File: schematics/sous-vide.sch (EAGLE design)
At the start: 30 parts, among them IC1 MEGA32-P

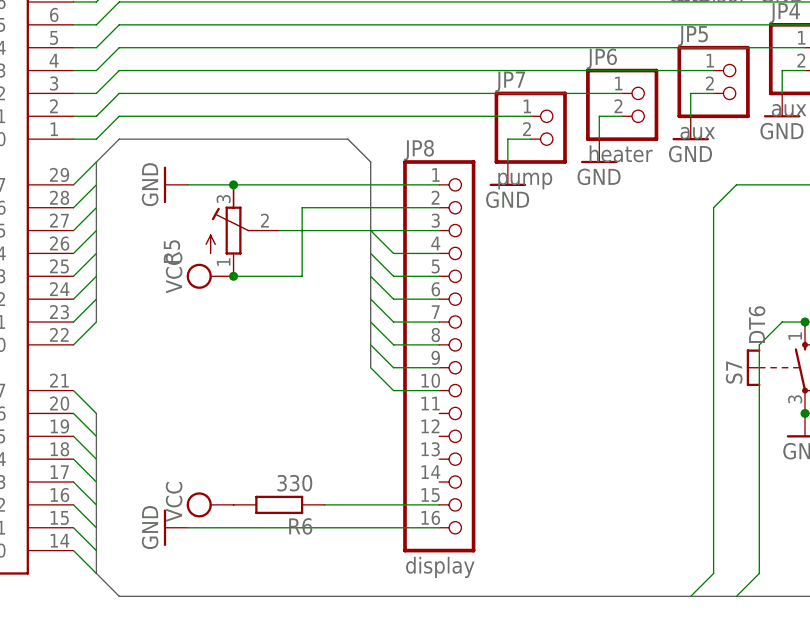
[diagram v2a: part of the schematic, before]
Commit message: initial steps to move from at32u4 naar at32
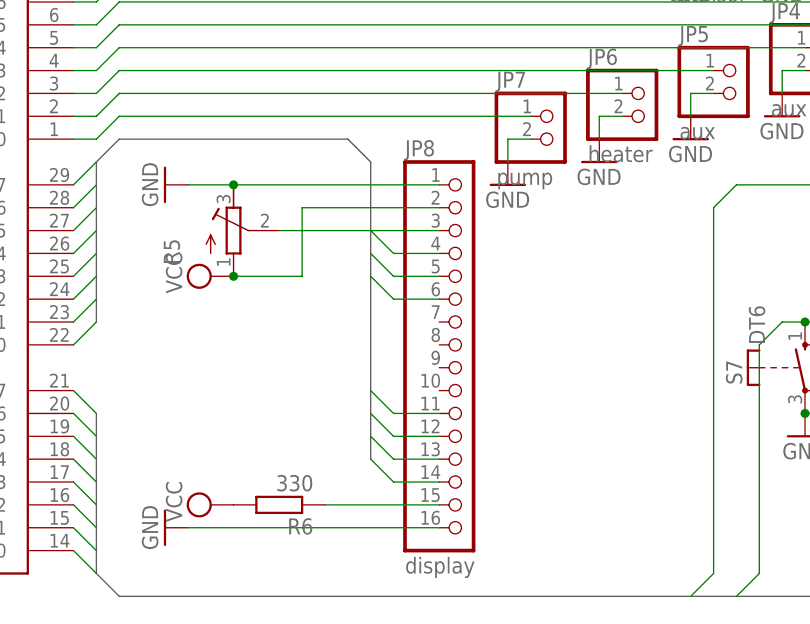
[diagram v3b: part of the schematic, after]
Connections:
- net DISPLAY4: now also JP8.11; no longer JP8.7
- net DISPLAY5: now also JP8.12; no longer JP8.8
- net DISPLAY6: now also JP8.13; no longer JP8.9
- net DISPLAY7: now also JP8.14; no longer JP8.10
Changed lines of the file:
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@@
 <wire x1="63.5" y1="55.88" x2="88.9" y2="55.88" width="0.762" layer="92"/>
 <wire x1="88.9" y1="55.88" x2="91.44" y2="53.34" width="0.762" layer="92"/>
-<wire x1="91.44" y1="53.34" x2="91.44" y2="30.48" width="0.762" layer="92"/>
+<wire x1="91.44" y1="53.34" x2="91.44" y2="20.32" width="0.762" layer="92"/>
 </segment>
 </bus>
@@
 </segment>
 <segment>
-<wire x1="91.44" y1="38.1" x2="93.98" y2="35.56" width="0.1524" layer="91"/>
-<pinref part="JP8" gate="A" pin="7"/>
-<wire x1="93.98" y1="35.56" x2="99.06" y2="35.56" width="0.1524" layer="91"/>
+<wire x1="91.44" y1="27.94" x2="93.98" y2="25.4" width="0.1524" layer="91"/>
+<pinref part="JP8" gate="A" pin="11"/>
+<wire x1="93.98" y1="25.4" x2="99.06" y2="25.4" width="0.1524" layer="91"/>
 </segment>
 </net>
@@
 </segment>
 <segment>
-<wire x1="91.44" y1="35.56" x2="93.98" y2="33.02" width="0.1524" layer="91"/>
-<pinref part="JP8" gate="A" pin="8"/>
-<wire x1="93.98" y1="33.02" x2="99.06" y2="33.02" width="0.1524" layer="91"/>
+<wire x1="91.44" y1="25.4" x2="93.98" y2="22.86" width="0.1524" layer="91"/>
+<pinref part="JP8" gate="A" pin="12"/>
+<wire x1="93.98" y1="22.86" x2="99.06" y2="22.86" width="0.1524" layer="91"/>
 </segment>
 </net>
@@
 </segment>
 <segment>
-<wire x1="91.44" y1="33.02" x2="93.98" y2="30.48" width="0.1524" layer="91"/>
-<pinref part="JP8" gate="A" pin="9"/>
-<wire x1="93.98" y1="30.48" x2="99.06" y2="30.48" width="0.1524" layer="91"/>
+<wire x1="91.44" y1="22.86" x2="93.98" y2="20.32" width="0.1524" layer="91"/>
+<pinref part="JP8" gate="A" pin="13"/>
+<wire x1="93.98" y1="20.32" x2="99.06" y2="20.32" width="0.1524" layer="91"/>
 </segment>
 </net>
@@
 </segment>
 <segment>
-<wire x1="91.44" y1="30.48" x2="93.98" y2="27.94" width="0.1524" layer="91"/>
-<pinref part="JP8" gate="A" pin="10"/>
-<wire x1="93.98" y1="27.94" x2="99.06" y2="27.94" width="0.1524" layer="91"/>
-</segment>
-</net>
+<wire x1="91.44" y1="20.32" x2="93.98" y2="17.78" width="0.1524" layer="91"/>
+<pinref part="JP8" gate="A" pin="14"/>
+<wire x1="93.98" y1="17.78" x2="99.06" y2="17.78" width="0.1524" layer="91"/>
+</segment>
+</net>

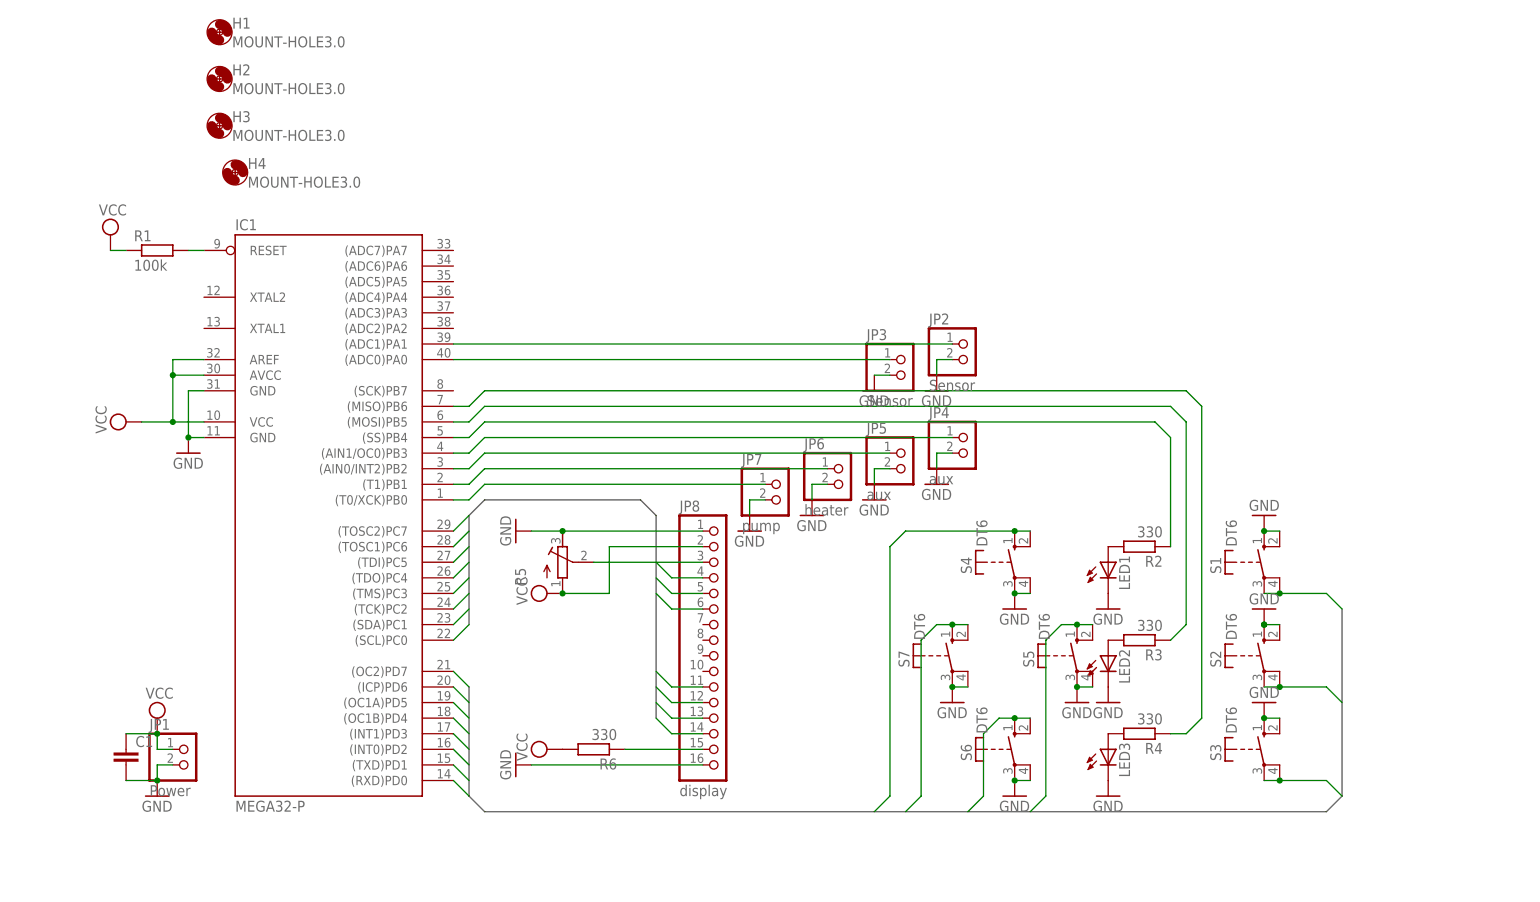
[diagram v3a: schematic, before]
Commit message: Average temp reading + ISP connector
Temp readings are averaged per second before comparing to the set
temperature. Added ISP header to board for on-board reprogramming.
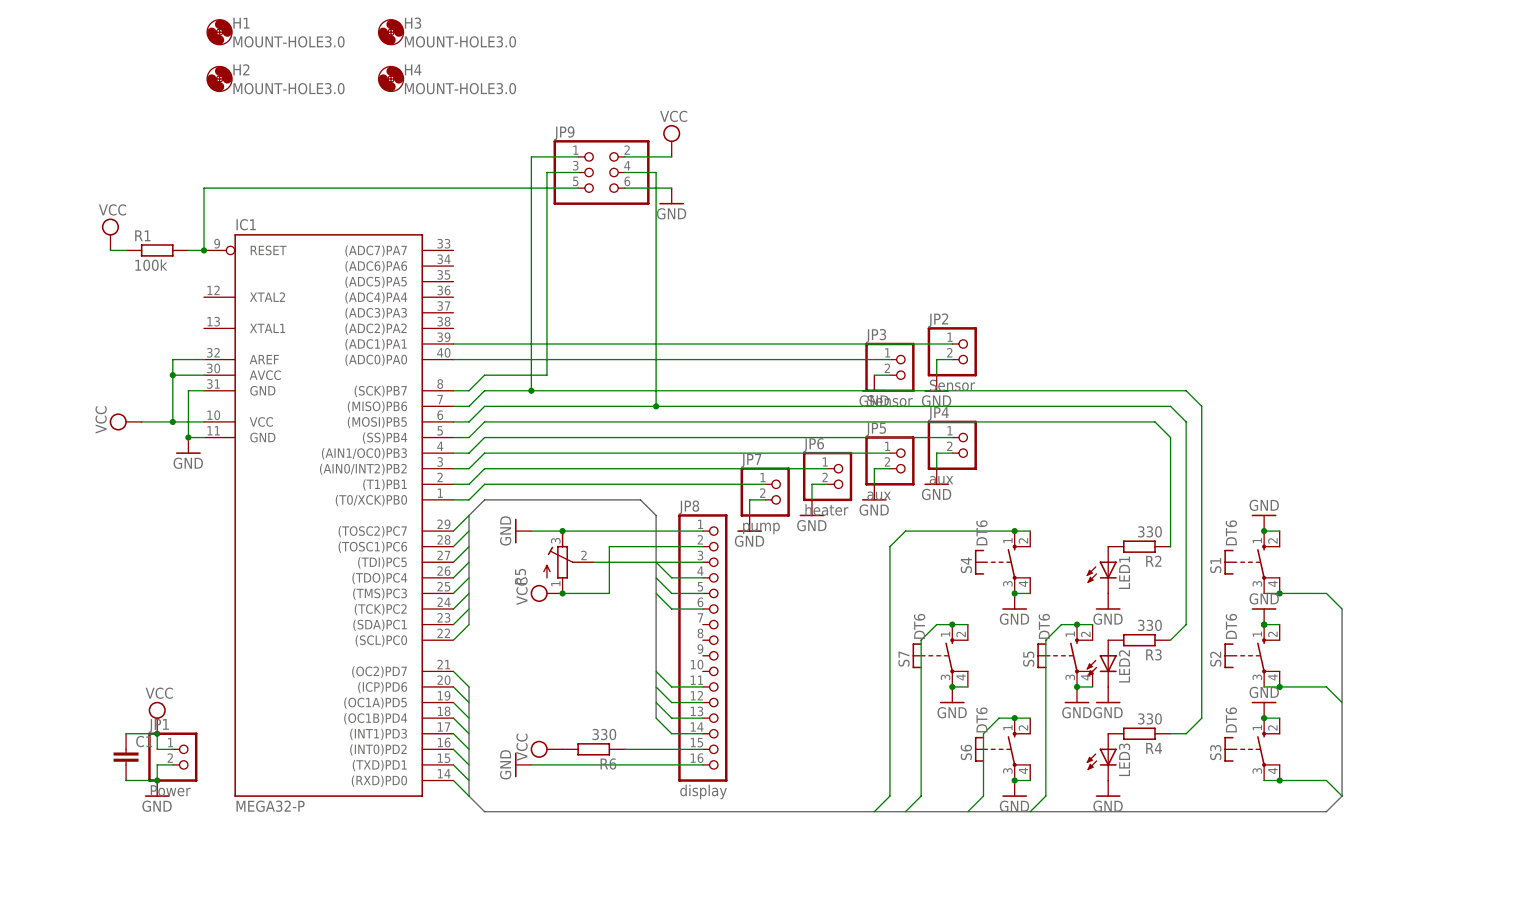
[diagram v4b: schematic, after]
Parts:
- added JP9: (no value), pinhead:PINHD-2X3
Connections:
- new net N$17: IC1.(SCK)PB7, JP9.3
- net GND: now also JP9.6
- net N$11: now also JP9.4
- net N$13: now also JP9.1
- net N$3: now also JP9.5
- net VCC: now also JP9.2
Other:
- moved on the sheet: H3, H4
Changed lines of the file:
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@@
 <part name="GND6" library="supply1" deviceset="GND" device=""/>
 <part name="GND7" library="supply1" deviceset="GND" device=""/>
+<part name="JP9" library="pinhead" deviceset="PINHD-2X3" device=""/>
+<part name="SUPPLY4" library="supply2" deviceset="VCC" device=""/>
+<part name="GND21" library="supply1" deviceset="GND" device=""/>
 </parts>
 <sheets>
@@
 <instance part="H1" gate="G$1" x="20.32" y="132.08"/>
 <instance part="H2" gate="G$1" x="20.32" y="124.46"/>
-<instance part="H3" gate="G$1" x="20.32" y="116.84"/>
-<instance part="H4" gate="G$1" x="22.86" y="109.22"/>
+<instance part="H3" gate="G$1" x="48.26" y="132.08"/>
+<instance part="H4" gate="G$1" x="48.26" y="124.46"/>
 <instance part="GND4" gate="1" x="149.86" y="38.1"/>
 <instance part="GND5" gate="1" x="139.7" y="22.86"/>
 <instance part="GND6" gate="1" x="160.02" y="22.86"/>
 <instance part="GND7" gate="1" x="149.86" y="7.62"/>
+<instance part="JP9" gate="A" x="81.28" y="109.22"/>
+<instance part="SUPPLY4" gate="G$1" x="93.98" y="114.3"/>
+<instance part="GND21" gate="1" x="93.98" y="104.14"/>
 </instances>
 <busses>
@@
 <junction x="149.86" y="10.16"/>
 </segment>
+<segment>
+<pinref part="JP9" gate="A" pin="6"/>
+<pinref part="GND21" gate="1" pin="GND"/>
+<wire x1="93.98" y1="106.68" x2="86.36" y2="106.68" width="0.1524" layer="91"/>
+</segment>
 </net>
 <net name="N$3" class="0">
@@
 <pinref part="R1" gate="G$1" pin="2"/>
 <wire x1="15.24" y1="96.52" x2="17.78" y2="96.52" width="0.1524" layer="91"/>
+<pinref part="JP9" gate="A" pin="5"/>
+<wire x1="78.74" y1="106.68" x2="17.78" y2="106.68" width="0.1524" layer="91"/>
+<wire x1="17.78" y1="106.68" x2="17.78" y2="96.52" width="0.1524" layer="91"/>
+<junction x="17.78" y="96.52"/>
 </segment>
 </net>
@@
 <pinref part="SUPPLY3" gate="G$1" pin="VCC"/>
 </segment>
+<segment>
+<pinref part="JP9" gate="A" pin="2"/>
+<pinref part="SUPPLY4" gate="G$1" pin="VCC"/>
+<wire x1="93.98" y1="111.76" x2="86.36" y2="111.76" width="0.1524" layer="91"/>
+</segment>
 </net>
 <net name="N$12" class="0">
@@
 <wire x1="58.42" y1="68.58" x2="60.96" y2="68.58" width="0.1524" layer="91"/>
 <wire x1="60.96" y1="68.58" x2="63.5" y2="71.12" width="0.1524" layer="91"/>
-<wire x1="63.5" y1="71.12" x2="175.26" y2="71.12" width="0.1524" layer="91"/>
+<wire x1="63.5" y1="71.12" x2="91.44" y2="71.12" width="0.1524" layer="91"/>
+<wire x1="91.44" y1="71.12" x2="175.26" y2="71.12" width="0.1524" layer="91"/>
 <wire x1="175.26" y1="71.12" x2="177.8" y2="68.58" width="0.1524" layer="91"/>
 <pinref part="R3" gate="G$1" pin="1"/>
 <wire x1="177.8" y1="68.58" x2="177.8" y2="35.56" width="0.1524" layer="91"/>
 <wire x1="177.8" y1="35.56" x2="175.26" y2="33.02" width="0.1524" layer="91"/>
+<pinref part="JP9" gate="A" pin="4"/>
+<wire x1="86.36" y1="109.22" x2="91.44" y2="109.22" width="0.1524" layer="91"/>
+<wire x1="91.44" y1="109.22" x2="91.44" y2="71.12" width="0.1524" layer="91"/>
+<junction x="91.44" y="71.12"/>
 </segment>
 </net>
@@
 <wire x1="180.34" y1="20.32" x2="180.34" y2="71.12" width="0.1524" layer="91"/>
 <wire x1="180.34" y1="71.12" x2="177.8" y2="73.66" width="0.1524" layer="91"/>
-<wire x1="177.8" y1="73.66" x2="63.5" y2="73.66" width="0.1524" layer="91"/>
+<wire x1="177.8" y1="73.66" x2="71.12" y2="73.66" width="0.1524" layer="91"/>
+<wire x1="71.12" y1="73.66" x2="63.5" y2="73.66" width="0.1524" layer="91"/>
 <wire x1="63.5" y1="73.66" x2="60.96" y2="71.12" width="0.1524" layer="91"/>
 <pinref part="IC1" gate="G$1" pin="(MISO)PB6"/>
 <wire x1="60.96" y1="71.12" x2="58.42" y2="71.12" width="0.1524" layer="91"/>
+<pinref part="JP9" gate="A" pin="1"/>
+<wire x1="78.74" y1="111.76" x2="71.12" y2="111.76" width="0.1524" layer="91"/>
+<wire x1="71.12" y1="111.76" x2="71.12" y2="73.66" width="0.1524" layer="91"/>
+<junction x="71.12" y="73.66"/>
 </segment>
 </net>
@@
 </segment>
 </net>
+<net name="N$17" class="0">
+<segment>
+<pinref part="JP9" gate="A" pin="3"/>
+<wire x1="78.74" y1="109.22" x2="73.66" y2="109.22" width="0.1524" layer="91"/>
+<wire x1="73.66" y1="109.22" x2="73.66" y2="76.2" width="0.1524" layer="91"/>
+<wire x1="73.66" y1="76.2" x2="63.5" y2="76.2" width="0.1524" layer="91"/>
+<wire x1="63.5" y1="76.2" x2="60.96" y2="73.66" width="0.1524" layer="91"/>
+<pinref part="IC1" gate="G$1" pin="(SCK)PB7"/>
+<wire x1="60.96" y1="73.66" x2="58.42" y2="73.66" width="0.1524" layer="91"/>
+</segment>
+</net>

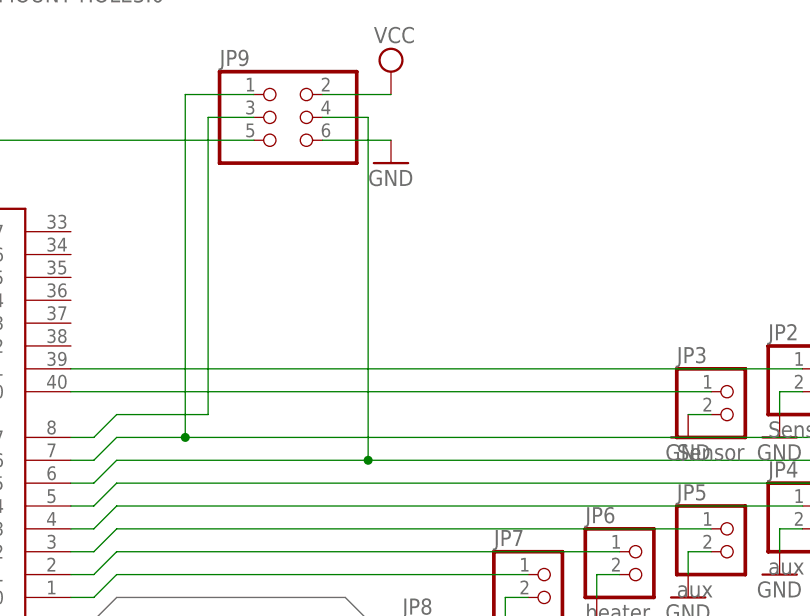
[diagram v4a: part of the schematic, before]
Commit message: Updated schematic and PCB
Now includes 4th led for reading indicator. Moved ISP connector to more
accessible location.
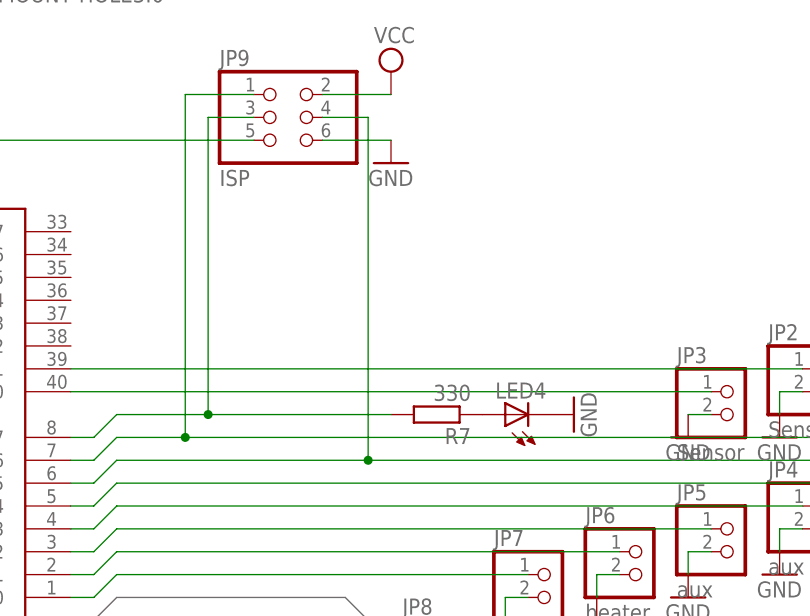
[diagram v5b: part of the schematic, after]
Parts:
- added LED4: (no value), led:LED3MM
- added R7: 330, rcl:R-EU_0207/2V
- JP9: value (none) -> ISP
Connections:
- new net N$16: LED4.A, R7.1
- net GND: now also LED4.C
- net N$17: now also R7.2
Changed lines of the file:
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@@
 <part name="GND6" library="supply1" deviceset="GND" device=""/>
 <part name="GND7" library="supply1" deviceset="GND" device=""/>
-<part name="JP9" library="pinhead" deviceset="PINHD-2X3" device=""/>
+<part name="JP9" library="pinhead" deviceset="PINHD-2X3" device="" value="ISP"/>
 <part name="SUPPLY4" library="supply2" deviceset="VCC" device=""/>
 <part name="GND21" library="supply1" deviceset="GND" device=""/>
+<part name="LED4" library="led" deviceset="LED" device="3MM"/>
+<part name="R7" library="rcl" deviceset="R-EU_" device="0207/2V" value="330"/>
+<part name="GND22" library="supply1" deviceset="GND" device=""/>
 </parts>
 <sheets>
@@
 <instance part="SUPPLY4" gate="G$1" x="93.98" y="114.3"/>
 <instance part="GND21" gate="1" x="93.98" y="104.14"/>
+<instance part="LED4" gate="G$1" x="106.68" y="76.2" rot="R90"/>
+<instance part="R7" gate="G$1" x="99.06" y="76.2" rot="R180"/>
+<instance part="GND22" gate="1" x="114.3" y="76.2" rot="R90"/>
 </instances>
 <busses>
@@
 <pinref part="GND21" gate="1" pin="GND"/>
 <wire x1="93.98" y1="106.68" x2="86.36" y2="106.68" width="0.1524" layer="91"/>
+</segment>
+<segment>
+<pinref part="LED4" gate="G$1" pin="C"/>
+<pinref part="GND22" gate="1" pin="GND"/>
 </segment>
 </net>
@@
 <pinref part="IC1" gate="G$1" pin="(SCK)PB7"/>
 <wire x1="60.96" y1="73.66" x2="58.42" y2="73.66" width="0.1524" layer="91"/>
-</segment>
-</net>
+<pinref part="R7" gate="G$1" pin="2"/>
+<wire x1="93.98" y1="76.2" x2="73.66" y2="76.2" width="0.1524" layer="91"/>
+<junction x="73.66" y="76.2"/>
+</segment>
+</net>
+<net name="N$16" class="0">
+<segment>
+<pinref part="R7" gate="G$1" pin="1"/>
+<pinref part="LED4" gate="G$1" pin="A"/>
+</segment>
+</net>
